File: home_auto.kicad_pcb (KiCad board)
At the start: 6 copper layers, 36.8 x 32.2 mm, 85 parts, among them J1 DF12NC_3.0_-60DS-0.5V_51_, J13 Conn_01x08_Pin, J2 DF12NC_3.0_-60DS-0.5V_51_, U1 RP115H331D, U3 RP115H181D, U4 LFMXO5-25

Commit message: relay unit
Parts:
- removed C13, C17, C18, C19, C20, C21, C22, C30, C31, C32, C33, C34, C35, C37, C38, C40, C41, C43, C45, C46, C47, C48, C49, C50, C52, C53, C55, C58, C59: 100n, Capacitor_SMD:C_0402_1005Metric
- removed C14, C24: 2.2u, Capacitor_SMD:C_0603_1608Metric
- removed C15, C28, C29, C36, C39, C51, C57, C60, C66: 10u, Capacitor_SMD:C_0603_1608Metric
- removed C16, C25, C26: 10u, Capacitor_SMD:C_0805_2012Metric
- removed C23, C27: 100n, Capacitor_SMD:C_0603_1608Metric
- removed C5: 0.1n, Capacitor_SMD:C_0603_1608Metric
- removed C6, C7: 22u, Capacitor_SMD:C_0805_2012Metric
- removed C8: 1u, Capacitor_SMD:C_0603_1608Metric
- removed C9: 3.3n, Capacitor_SMD:C_0603_1608Metric
- removed L1: SPM6530T-1R5M-HZ, SPM6530T-1R5M-HZ:SPM6530
- removed L10, L11, L2, L7, L9: MPZ1005S121CT000, Inductor_SMD:L_0402_1005Metric
- removed PS1: BD9D321EFJ-E2, BD9D321EFJ-E2:SOIC127P600X100-8N
- removed R184, R185: 1k, Resistor_SMD:R_0402_1005Metric
- removed R186, R187, R188, R189: 4.7k, Resistor_SMD:R_0402_1005Metric
- removed R190: 0R, Resistor_SMD:R_0603_1608Metric
- removed U3: RP115H181D, Package_TO_SOT_SMD:SOT-89-5
- removed U4: LFMXO5-25, Package_BGA:BGA-256_14.0x14.0mm_Layout16x16_P0.8mm_Ball0.45mm_Pad0.32mm_NSMD
- added D1: D_Zener_Dual_CommonCathode_AAK, Package_TO_SOT_SMD:SOT-23, B.Cu at (183.7, 75.1)
- added D10: D_Zener_Dual_CommonCathode_AAK, Package_TO_SOT_SMD:SOT-23, B.Cu at (163.8, 106.6)
- added D11: D_Zener_Dual_CommonCathode_AAK, Package_TO_SOT_SMD:SOT-23, B.Cu at (148.0, 106.6)
- added D12: D_Zener_Dual_CommonCathode_AAK, Package_TO_SOT_SMD:SOT-23, B.Cu at (195.5, 106.6)
- added D13: D_Zener_Dual_CommonCathode_AAK, Package_TO_SOT_SMD:SOT-23, B.Cu at (152.1, 75.0)
- added D14: D_Zener_Dual_CommonCathode_AAK, Package_TO_SOT_SMD:SOT-23, B.Cu at (136.2, 75.0)
- added D15: 5.0SMDJ6.0CAS, 5_0SMDJ6_0CAS:DIONM7959X262N, F.Cu at (73.1, 73.7)
- added D2: D_Zener_Dual_CommonCathode_AAK, Package_TO_SOT_SMD:SOT-23, B.Cu at (212.0, 75.1)
- added D3: D_Zener_Dual_CommonCathode_AAK, Package_TO_SOT_SMD:SOT-23, B.Cu at (167.9, 75.1)
- added D4: D_Zener_Dual_CommonCathode_AAK, Package_TO_SOT_SMD:SOT-23, B.Cu at (243.7, 75.2)
- added D5: D_Zener_Dual_CommonCathode_AAK, Package_TO_SOT_SMD:SOT-23, B.Cu at (227.9, 75.2)
- added D6: D_Zener_Dual_CommonCathode_AAK, Package_TO_SOT_SMD:SOT-23, B.Cu at (227.2, 106.6)
- added D7: D_Zener_Dual_CommonCathode_AAK, Package_TO_SOT_SMD:SOT-23, B.Cu at (243.0, 106.6)
- added D8: D_Zener_Dual_CommonCathode_AAK, Package_TO_SOT_SMD:SOT-23, B.Cu at (179.6, 106.6)
- added D9: D_Zener_Dual_CommonCathode_AAK, Package_TO_SOT_SMD:SOT-23, B.Cu at (211.3, 106.6)
- added J10: TC0203620000G, KiCad:TC0203620000G, F.Cu at (186.2, 46.5)
- added J11: TC0203620000G, KiCad:TC0203620000G, F.Cu at (214.5, 46.5)
- added J12: TC0203620000G, KiCad:TC0203620000G, F.Cu at (170.4, 46.4)
- added J14: TC0203620000G, KiCad:TC0203620000G, F.Cu at (230.3, 46.6)
- added J15: TC0203620000G, KiCad:TC0203620000G, F.Cu at (224.7, 135.3)
- added J16: TC0203620000G, KiCad:TC0203620000G, F.Cu at (240.5, 135.2)
- added J17: TC0203620000G, KiCad:TC0203620000G, F.Cu at (177.1, 135.2)
- added J18: TC0203620000G, KiCad:TC0203620000G, F.Cu at (208.9, 135.3)
- added J19: TC0203620000G, KiCad:TC0203620000G, F.Cu at (161.3, 135.3)
- added J20: TC0203620000G, KiCad:TC0203620000G, F.Cu at (145.5, 135.2)
- added J21: TC0203620000G, KiCad:TC0203620000G, F.Cu at (193.0, 135.2)
- added J22: TC0203620000G, KiCad:TC0203620000G, F.Cu at (154.5, 46.4)
- added J23: TC0203620000G, KiCad:TC0203620000G, F.Cu at (138.7, 46.4)
- added J24: Conn_01x02_Pin, Connector_PinHeader_1.27mm:PinHeader_1x02_P1.27mm_Vertical, F.Cu at (79.2, 66.2)
- added J25: Conn_01x04_Pin, Connector_PinHeader_1.27mm:PinHeader_1x04_P1.27mm_Vertical, F.Cu at (80.9, 56.6)
- added J26: Conn_01x02_Pin, Connector_PinHeader_1.27mm:PinHeader_1x02_P1.27mm_Vertical, F.Cu at (76.7, 56.6)
- added J27: TC0203620000G, KiCad:TC0203620000G, F.Cu at (60.6, 68.3)
- added J3: TC0203620000G, KiCad:TC0203620000G, F.Cu at (124.0, 61.3)
- added J4: Conn_02x10_Top_Bottom, Connector_PinHeader_2.54mm:PinHeader_2x10_P2.54mm_Vertical_SMD, F.Cu at (72.6, 107.7)
- added J5: Conn_02x10_Top_Bottom, Connector_PinHeader_2.54mm:PinHeader_2x10_P2.54mm_Vertical_SMD, F.Cu at (77.5, 90.2)
- added J6: TC0203620000G, KiCad:TC0203620000G, F.Cu at (256.7, 61.3)
- added J7: TC0203620000G, KiCad:TC0203620000G, F.Cu at (135.0, 117.5)
- added J8: TC0203620000G, KiCad:TC0203620000G, F.Cu at (256.2, 124.6)
- added J9: Conn_01x08_Pin, Connector_PinHeader_1.27mm:PinHeader_1x08_P1.27mm_Vertical, F.Cu at (233.5, 86.1)
- added K1: G5NB-1A4_DC5, G5NB-1A4_DC5:G5NB1A4DC5, F.Cu at (179.7, 72.5)
- added K10: G5NB-1A4_DC5, G5NB-1A4_DC5:G5NB1A4DC5, F.Cu at (231.8, 72.6)
- added K11: G5NB-1A4_DC5, G5NB-1A4_DC5:G5NB1A4DC5, F.Cu at (231.2, 109.2)
- added K12: G5NB-1A4_DC5, G5NB-1A4_DC5:G5NB1A4DC5, F.Cu at (223.3, 109.2)
- added K13: G5NB-1A4_DC5, G5NB-1A4_DC5:G5NB1A4DC5, F.Cu at (247.0, 109.2)
- added K14: G5NB-1A4_DC5, G5NB-1A4_DC5:G5NB1A4DC5, F.Cu at (239.1, 109.2)
- added K15: G5NB-1A4_DC5, G5NB-1A4_DC5:G5NB1A4DC5, F.Cu at (183.6, 109.2)
- added K16: G5NB-1A4_DC5, G5NB-1A4_DC5:G5NB1A4DC5, F.Cu at (175.7, 109.2)
- added K17: G5NB-1A4_DC5, G5NB-1A4_DC5:G5NB1A4DC5, F.Cu at (215.3, 109.2)
- added K18: G5NB-1A4_DC5, G5NB-1A4_DC5:G5NB1A4DC5, F.Cu at (207.4, 109.2)
- added K19: G5NB-1A4_DC5, G5NB-1A4_DC5:G5NB1A4DC5, F.Cu at (167.8, 109.2)
- added K2: G5NB-1A4_DC5, G5NB-1A4_DC5:G5NB1A4DC5, F.Cu at (187.6, 72.5)
- added K20: G5NB-1A4_DC5, G5NB-1A4_DC5:G5NB1A4DC5, F.Cu at (159.9, 109.2)
- added K21: G5NB-1A4_DC5, G5NB-1A4_DC5:G5NB1A4DC5, F.Cu at (152.0, 109.2)
- added K22: G5NB-1A4_DC5, G5NB-1A4_DC5:G5NB1A4DC5, F.Cu at (144.1, 109.2)
- added K23: G5NB-1A4_DC5, G5NB-1A4_DC5:G5NB1A4DC5, F.Cu at (199.5, 109.2)
- added K24: G5NB-1A4_DC5, G5NB-1A4_DC5:G5NB1A4DC5, F.Cu at (191.6, 109.2)
- added K25: G5NB-1A4_DC5, G5NB-1A4_DC5:G5NB1A4DC5, F.Cu at (148.1, 72.5)
- added K26: G5NB-1A4_DC5, G5NB-1A4_DC5:G5NB1A4DC5, F.Cu at (156.0, 72.5)
- added K27: G5NB-1A4_DC5, G5NB-1A4_DC5:G5NB1A4DC5, F.Cu at (132.2, 72.4)
- added K28: G5NB-1A4_DC5, G5NB-1A4_DC5:G5NB1A4DC5, F.Cu at (140.2, 72.4)
- added K3: G5NB-1A4_DC5, G5NB-1A4_DC5:G5NB1A4DC5, F.Cu at (208.0, 72.5)
- added K4: G5NB-1A4_DC5, G5NB-1A4_DC5:G5NB1A4DC5, F.Cu at (215.9, 72.5)
- added K5: G5NB-1A4_DC5, G5NB-1A4_DC5:G5NB1A4DC5, F.Cu at (163.9, 72.5)
- added K6: G5NB-1A4_DC5, G5NB-1A4_DC5:G5NB1A4DC5, F.Cu at (171.8, 72.5)
- added K7: G5NB-1A4_DC5, G5NB-1A4_DC5:G5NB1A4DC5, F.Cu at (239.7, 72.7)
- added K8: G5NB-1A4_DC5, G5NB-1A4_DC5:G5NB1A4DC5, F.Cu at (247.6, 72.7)
- added K9: G5NB-1A4_DC5, G5NB-1A4_DC5:G5NB1A4DC5, F.Cu at (223.9, 72.6)
- added Q1: BC849, Package_TO_SOT_SMD:SOT-23, B.Cu at (177.6, 75.1)
- added Q10: BC849, Package_TO_SOT_SMD:SOT-23, B.Cu at (233.9, 75.2)
- added Q11: BC849, Package_TO_SOT_SMD:SOT-23, B.Cu at (233.3, 106.6)
- added Q12: BC849, Package_TO_SOT_SMD:SOT-23, B.Cu at (221.1, 106.6)
- added Q13: BC849, Package_TO_SOT_SMD:SOT-23, B.Cu at (249.0, 106.6)
- added Q14: BC849, Package_TO_SOT_SMD:SOT-23, B.Cu at (236.9, 106.6)
- added Q15: BC849, Package_TO_SOT_SMD:SOT-23, B.Cu at (185.7, 106.6)
- added Q16: BC849, Package_TO_SOT_SMD:SOT-23, B.Cu at (173.5, 106.6)
- added Q17: BC849, Package_TO_SOT_SMD:SOT-23, B.Cu at (217.4, 106.6)
- added Q18: BC849, Package_TO_SOT_SMD:SOT-23, B.Cu at (205.3, 106.6)
- added Q19: BC849, Package_TO_SOT_SMD:SOT-23, B.Cu at (169.9, 106.6)
- added Q2: BC849, Package_TO_SOT_SMD:SOT-23, B.Cu at (189.8, 75.1)
- added Q20: BC849, Package_TO_SOT_SMD:SOT-23, B.Cu at (157.7, 106.6)
- added Q21: BC849, Package_TO_SOT_SMD:SOT-23, B.Cu at (154.1, 106.6)
- added Q22: BC849, Package_TO_SOT_SMD:SOT-23, B.Cu at (141.9, 106.6)
- added Q23: BC849, Package_TO_SOT_SMD:SOT-23, B.Cu at (201.5, 106.6)
- added Q24: BC849, Package_TO_SOT_SMD:SOT-23, B.Cu at (189.4, 106.6)
- added Q25: BC849, Package_TO_SOT_SMD:SOT-23, B.Cu at (146.0, 75.0)
- added Q26: BC849, Package_TO_SOT_SMD:SOT-23, B.Cu at (158.1, 75.0)
- added Q27: BC849, Package_TO_SOT_SMD:SOT-23, B.Cu at (130.2, 75.0)
- added Q28: BC849, Package_TO_SOT_SMD:SOT-23, B.Cu at (142.3, 75.0)
- added Q3: BC849, Package_TO_SOT_SMD:SOT-23, B.Cu at (205.9, 75.1)
- added Q4: BC849, Package_TO_SOT_SMD:SOT-23, B.Cu at (218.1, 75.1)
- added Q5: BC849, Package_TO_SOT_SMD:SOT-23, B.Cu at (161.8, 75.1)
- added Q6: BC849, Package_TO_SOT_SMD:SOT-23, B.Cu at (174.0, 75.1)
- added Q7: BC849, Package_TO_SOT_SMD:SOT-23, B.Cu at (237.6, 75.2)
- added Q8: BC849, Package_TO_SOT_SMD:SOT-23, B.Cu at (249.8, 75.2)
- added Q9: BC849, Package_TO_SOT_SMD:SOT-23, B.Cu at (221.8, 75.2)
- added R14: 4K7, Resistor_SMD:R_0603_1608Metric, F.Cu at (201.7, 86.1)
- added R15: 0R, Resistor_SMD:R_0805_2012Metric, F.Cu at (230.4, 84.3)
- added R16: 4K7, Resistor_SMD:R_0603_1608Metric, F.Cu at (207.9, 98.0)
- added R17: 4K7, Resistor_SMD:R_0603_1608Metric, F.Cu at (200.3, 86.1)
- added R18: 0R, Resistor_SMD:R_0603_1608Metric, F.Cu at (226.9, 85.1)
- added R19: 4K7, Resistor_SMD:R_0603_1608Metric, F.Cu at (209.4, 98.0)
- added R20: 4K7, Resistor_SMD:R_0603_1608Metric, F.Cu at (198.8, 86.1)
- added R21: 4K7, Resistor_SMD:R_0603_1608Metric, F.Cu at (210.9, 98.0)
- added R22: 4K7, Resistor_SMD:R_0603_1608Metric, F.Cu at (197.3, 86.1)
- added R23: 10k, Resistor_SMD:R_0603_1608Metric, B.Cu at (180.8, 75.5)
- added R24: 10k, Resistor_SMD:R_0603_1608Metric, B.Cu at (186.8, 75.5)
- added R25: 10k, Resistor_SMD:R_0603_1608Metric, B.Cu at (209.1, 75.5)
- added R26: 10k, Resistor_SMD:R_0603_1608Metric, B.Cu at (215.1, 75.5)
- added R27: 10k, Resistor_SMD:R_0603_1608Metric, B.Cu at (164.9, 75.5)
- added R28: 10k, Resistor_SMD:R_0603_1608Metric, B.Cu at (171.0, 75.5)
- added R29: 10k, Resistor_SMD:R_0603_1608Metric, B.Cu at (240.7, 75.7)
- added R30: 10k, Resistor_SMD:R_0603_1608Metric, B.Cu at (246.8, 75.7)
- added R31: 10k, Resistor_SMD:R_0603_1608Metric, B.Cu at (224.9, 75.6)
- added R32: 10k, Resistor_SMD:R_0603_1608Metric, B.Cu at (231.0, 75.6)
- added R33: 10k, Resistor_SMD:R_0603_1608Metric, B.Cu at (230.2, 106.2)
- added R34: 10k, Resistor_SMD:R_0603_1608Metric, B.Cu at (224.1, 106.2)
- added R35: 10k, Resistor_SMD:R_0603_1608Metric, B.Cu at (245.9, 106.2)
- added R36: 10k, Resistor_SMD:R_0603_1608Metric, B.Cu at (239.8, 106.2)
- added R37: 10k, Resistor_SMD:R_0603_1608Metric, B.Cu at (182.6, 106.2)
- added R38: 10k, Resistor_SMD:R_0603_1608Metric, B.Cu at (176.5, 106.2)
- added R39: 10k, Resistor_SMD:R_0603_1608Metric, B.Cu at (214.3, 106.2)
- added R40: 10k, Resistor_SMD:R_0603_1608Metric, B.Cu at (208.2, 106.2)
- added R41: 10k, Resistor_SMD:R_0603_1608Metric, B.Cu at (166.8, 106.2)
- added R42: 10k, Resistor_SMD:R_0603_1608Metric, B.Cu at (160.7, 106.2)
- added R43: 10k, Resistor_SMD:R_0603_1608Metric, B.Cu at (151.0, 106.2)
- added R44: 10k, Resistor_SMD:R_0603_1608Metric, B.Cu at (144.9, 106.2)
- added R45: 10k, Resistor_SMD:R_0603_1608Metric, B.Cu at (198.4, 106.2)
- added R46: 10k, Resistor_SMD:R_0603_1608Metric, B.Cu at (192.3, 106.2)
- added R47: 10k, Resistor_SMD:R_0603_1608Metric, B.Cu at (149.1, 75.5)
- added R48: 10k, Resistor_SMD:R_0603_1608Metric, B.Cu at (155.2, 75.5)
- added R49: 10k, Resistor_SMD:R_0603_1608Metric, B.Cu at (133.3, 75.4)
- added R50: 10k, Resistor_SMD:R_0603_1608Metric, B.Cu at (139.4, 75.4)
- added R51: 10k, Resistor_SMD:R_0603_1608Metric, F.Cu at (251.4, 103.6)
- added R52: 10k, Resistor_SMD:R_0603_1608Metric, F.Cu at (252.0, 78.5)
- added R53: 10k, Resistor_SMD:R_0603_1608Metric, F.Cu at (245.6, 98.6)
- added R54: 10k, Resistor_SMD:R_0603_1608Metric, F.Cu at (67.9, 63.6)
- added R55: 10k, Resistor_SMD:R_0603_1608Metric, F.Cu at (67.9, 66.1)
- added R8: 4K7, Resistor_SMD:R_0603_1608Metric, F.Cu at (206.1, 86.1)
- added R9: 4K7, Resistor_SMD:R_0603_1608Metric, F.Cu at (203.3, 98.0)
- added SW1: SW_Omron_B3FS, Button_Switch_SMD:SW_SPST_Omron_B3FS-105xP, F.Cu at (240.5, 85.3)
- added U2: ESP32-C3-WROOM-02, RF_Module:ESP32-C3-WROOM-02, F.Cu at (254.1, 90.6)
- C1: value 10u -> 100n; footprint Capacitor_SMD:C_0805_2012Metric -> Capacitor_SMD:C_0603_1608Metric; moved to F.Cu
- C2: value 10u -> 100n; footprint Capacitor_SMD:C_0805_2012Metric -> Capacitor_SMD:C_0603_1608Metric
- C3: value 1u -> 100n; footprint Capacitor_SMD:C_0402_1005Metric -> Capacitor_SMD:C_0603_1608Metric
- C4: value 100n -> 1u; footprint Capacitor_SMD:C_0402_1005Metric -> Capacitor_SMD:C_0603_1608Metric; moved to F.Cu
- J1, J2: value DF12NC_3.0_-60DS-0.5V_51_ -> TC0203620000G; footprint DF12NC_3.0_60DS-0.5V:HRS_DF12NC_3.0_-60DS-0.5V_51_ -> KiCad:TC0203620000G; moved to F.Cu
- J13: value Conn_01x08_Pin -> TC0203620000G; footprint Connector_PinHeader_1.27mm:PinHeader_1x08_P1.27mm_Vertical -> KiCad:TC0203620000G; moved to F.Cu
- R1: value 4.7k -> 4K7; moved to F.Cu
- R10, R4: value 4.7k -> 4K7
- R11, R13, R5, R7: value 0R -> 4K7
- R12, R6: value 29.7k -> 4K7
- R2: value 7.5k -> 4K7
- R3: value 22k -> 4K7
- U1: value RP115H331D -> MACHox5_board; footprint Package_TO_SOT_SMD:SOT-89-5 -> machox5_board:machox5_board
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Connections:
- C1 pad 1: +5V -> /ESP32/EN
- C2 pad 1: +5V -> +3V3_ESP
- C3 pad 1: +5V -> +3V3_ESP
- C4 pad 1: Net-(PS1-BOOT) -> /ESP32/EN
- C4 pad 2: Net-(PS1-SW) -> GND
- J1 pad 1: +1V8 -> 230VAC
- J1 pad 2: +3V3 -> 230VAC
- J13 pad 1: +3V3_BANK -> /led_cluster/led_cur_lim3/UP_OUT
- J13 pad 2: /FPGA_machX05/FTDI/NX_TDO -> /led_cluster/led_cur_lim3/DOWN_OUT
- J2 pad 1: GND -> 230VAC
- J2 pad 2: GND -> 230VAC
- R1 pad 1: +5V -> /sw_10
- R1 pad 2: Net-(PS1-EN) -> +UP
- R10 pad 1: +5V -> /sw_4
- R10 pad 2: Net-(U3-CE) -> +UP
- R11 pad 1: Net-(U3-VFB) -> /sw_15
- R11 pad 2: +1V8 -> +UP
- R12 pad 1: GND -> /sw_5
- R12 pad 2: Net-(U3-VFB) -> +UP
- R13 pad 1: Net-(U4N-VCCADC18) -> /sw_16
- R13 pad 2: GND -> +UP
- R2 pad 1: Net-(PS1-FB) -> /sw_0
- R2 pad 2: +1V0 -> +UP
- R3 pad 1: GND_DCDC -> /sw_11
- R3 pad 2: Net-(PS1-FB) -> +UP
- R4 pad 1: +5V -> /sw_1
- R4 pad 2: Net-(U1-CE) -> +UP
- R5 pad 1: Net-(U1-VFB) -> /sw_12
- R5 pad 2: +3V3 -> +UP
- R6 pad 1: GND -> /sw_2
- R6 pad 2: Net-(U1-VFB) -> +UP
- R7 pad 1: GND -> /sw_13
- R7 pad 2: GND_DCDC -> +UP
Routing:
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- added copper zone on F.Cu, net +UP
- added copper zone on B.Cu, net /led_cluster/led_cur_lim/DOWN_OUT
- added copper zone on F.Cu, net /led_cluster/led_cur_lim/DOWN_OUT
- added copper zone on B.Cu, net /led_cluster/led_cur_lim/UP_OUT
- added copper zone on F.Cu, net /led_cluster/led_cur_lim/UP_OUT
- added copper zone on B.Cu, net /led_cluster/led_cur_lim1/DOWN_OUT
- added copper zone on F.Cu, net /led_cluster/led_cur_lim1/DOWN_OUT
- added copper zone on B.Cu, net /led_cluster/led_cur_lim1/UP_OUT
- added copper zone on F.Cu, net /led_cluster/led_cur_lim1/UP_OUT
- added copper zone on B.Cu, net /led_cluster/led_cur_lim2/DOWN_OUT
- added copper zone on F.Cu, net /led_cluster/led_cur_lim2/DOWN_OUT
- added copper zone on B.Cu, net /led_cluster/led_cur_lim2/UP_OUT
- added copper zone on F.Cu, net /led_cluster/led_cur_lim2/UP_OUT
- added copper zone on B.Cu, net /led_cluster/led_cur_lim3/DOWN_OUT
- added copper zone on F.Cu, net /led_cluster/led_cur_lim3/DOWN_OUT
- added copper zone on B.Cu, net /led_cluster/led_cur_lim3/UP_OUT
- added copper zone on F.Cu, net /led_cluster/led_cur_lim3/UP_OUT
- added copper zone on B.Cu, net /led_cluster/led_cur_lim4/DOWN_OUT
- added copper zone on F.Cu, net /led_cluster/led_cur_lim4/DOWN_OUT
- added copper zone on B.Cu, net /led_cluster/led_cur_lim4/UP_OUT
- added copper zone on F.Cu, net /led_cluster/led_cur_lim4/UP_OUT
- added copper zone on B.Cu, net /led_cluster1/led_cur_lim/DOWN_OUT
- added copper zone on F.Cu, net /led_cluster1/led_cur_lim/DOWN_OUT
- added copper zone on B.Cu, net /led_cluster1/led_cur_lim/UP_OUT
- added copper zone on F.Cu, net /led_cluster1/led_cur_lim/UP_OUT
- added copper zone on B.Cu, net /led_cluster1/led_cur_lim1/DOWN_OUT
- added copper zone on F.Cu, net /led_cluster1/led_cur_lim1/DOWN_OUT
- added copper zone on B.Cu, net /led_cluster1/led_cur_lim1/UP_OUT
- added copper zone on F.Cu, net /led_cluster1/led_cur_lim1/UP_OUT
- added copper zone on B.Cu, net /led_cluster1/led_cur_lim2/DOWN_OUT
- added copper zone on F.Cu, net /led_cluster1/led_cur_lim2/DOWN_OUT
- added copper zone on B.Cu, net /led_cluster1/led_cur_lim2/UP_OUT
- added copper zone on F.Cu, net /led_cluster1/led_cur_lim2/UP_OUT
- added copper zone on B.Cu, net /led_cluster1/led_cur_lim3/DOWN_OUT
- added copper zone on F.Cu, net /led_cluster1/led_cur_lim3/DOWN_OUT
- added copper zone on B.Cu, net /led_cluster1/led_cur_lim3/UP_OUT
- added copper zone on F.Cu, net /led_cluster1/led_cur_lim3/UP_OUT
- added copper zone on B.Cu, net /led_cluster1/led_cur_lim4/DOWN_OUT
- added copper zone on F.Cu, net /led_cluster1/led_cur_lim4/DOWN_OUT
- added copper zone on B.Cu, net /led_cluster1/led_cur_lim4/UP_OUT
- added copper zone on F.Cu, net /led_cluster1/led_cur_lim4/UP_OUT
- added copper zone on B.Cu, net /led_cur_lim5/DOWN_OUT
- added copper zone on F.Cu, net /led_cur_lim5/DOWN_OUT
- added copper zone on B.Cu, net /led_cur_lim5/UP_OUT
- added copper zone on F.Cu, net /led_cur_lim5/UP_OUT
- added copper zone on B.Cu, net /led_cur_lim7/DOWN_OUT
- added copper zone on F.Cu, net /led_cur_lim7/DOWN_OUT
- added copper zone on B.Cu, net /led_cur_lim7/UP_OUT
- added copper zone on F.Cu, net /led_cur_lim7/UP_OUT
- added copper zone on B.Cu, net /led_cur_lim8/DOWN_OUT
- added copper zone on F.Cu, net /led_cur_lim8/DOWN_OUT
- added copper zone on B.Cu, net /led_cur_lim8/UP_OUT
- added copper zone on F.Cu, net /led_cur_lim8/UP_OUT
- added copper zone on F.Cu, net 230VAC
- removed copper zone on B.Cu, net +1V0
- removed copper zone on F.Cu, net +1V0
- removed copper zone on In2.Cu, net +1V0
- removed copper zone on B.Cu, net +1V8
- removed copper zone on F.Cu, net +1V8
- removed copper zone on In3.Cu, net +1V8
- removed copper zone on F.Cu, net +1V8_BANK
- removed copper zone on In2.Cu, net +1V8_BANK
- removed copper zone on In3.Cu, net +1V8_BANK
- removed copper zone on B.Cu, net +3V3
- removed copper zone on F.Cu, net +3V3
- removed copper zone on In2.Cu, net +3V3
- removed copper zone on F.Cu, net +3V3_BANK
- removed copper zone on In2.Cu, net +3V3_BANK
- removed copper zone on In3.Cu, net +3V3_BANK
- removed copper zone on B.Cu, net +5V
- removed copper zone on F.Cu, net +5V
- removed copper zone on In2.Cu, net +5V
- removed copper zone on In3.Cu, net +5V
- removed copper zone on B.Cu, net GND
- removed copper zone on F.Cu, net GND
- removed copper zone on In1.Cu, net GND
- removed copper zone on In2.Cu, net GND
- removed copper zone on In3.Cu, net GND
- removed copper zone on In4.Cu, net GND
- removed copper zone on F.Cu, net GND_DCDC
- removed copper zone on F.Cu, net Net-(PS1-SW)
- removed copper zone on F.Cu, net VCC_AUX
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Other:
- board size 36.8 x 32.2 mm -> 142.4 x 97.4 mm
- copper layers 6 -> 2

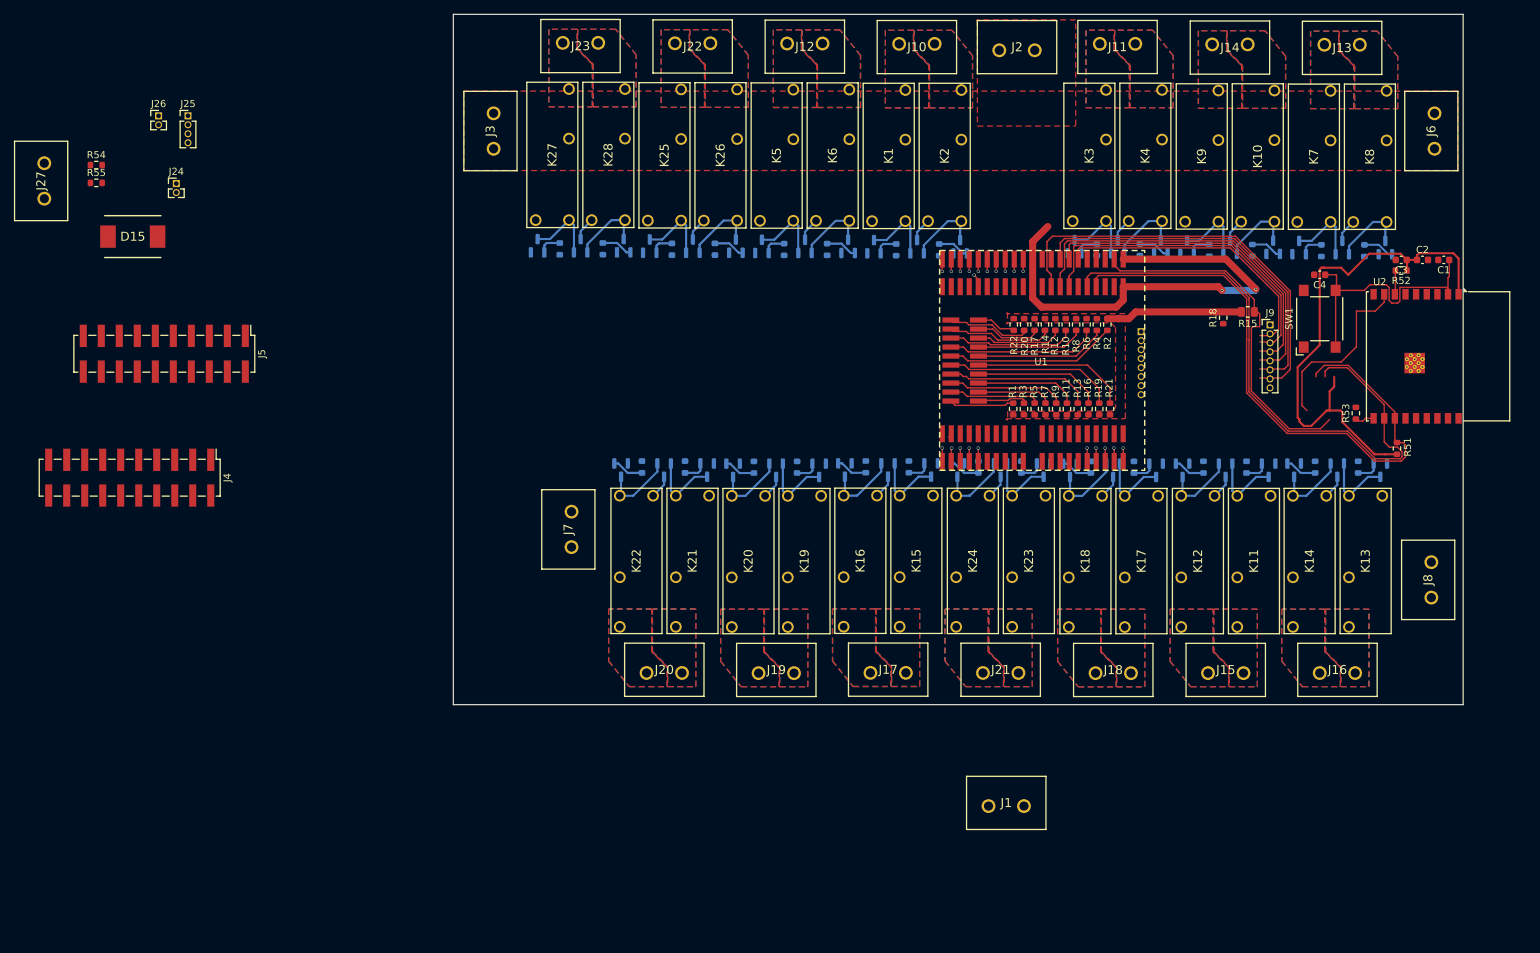
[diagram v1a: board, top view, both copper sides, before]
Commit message: relay placment
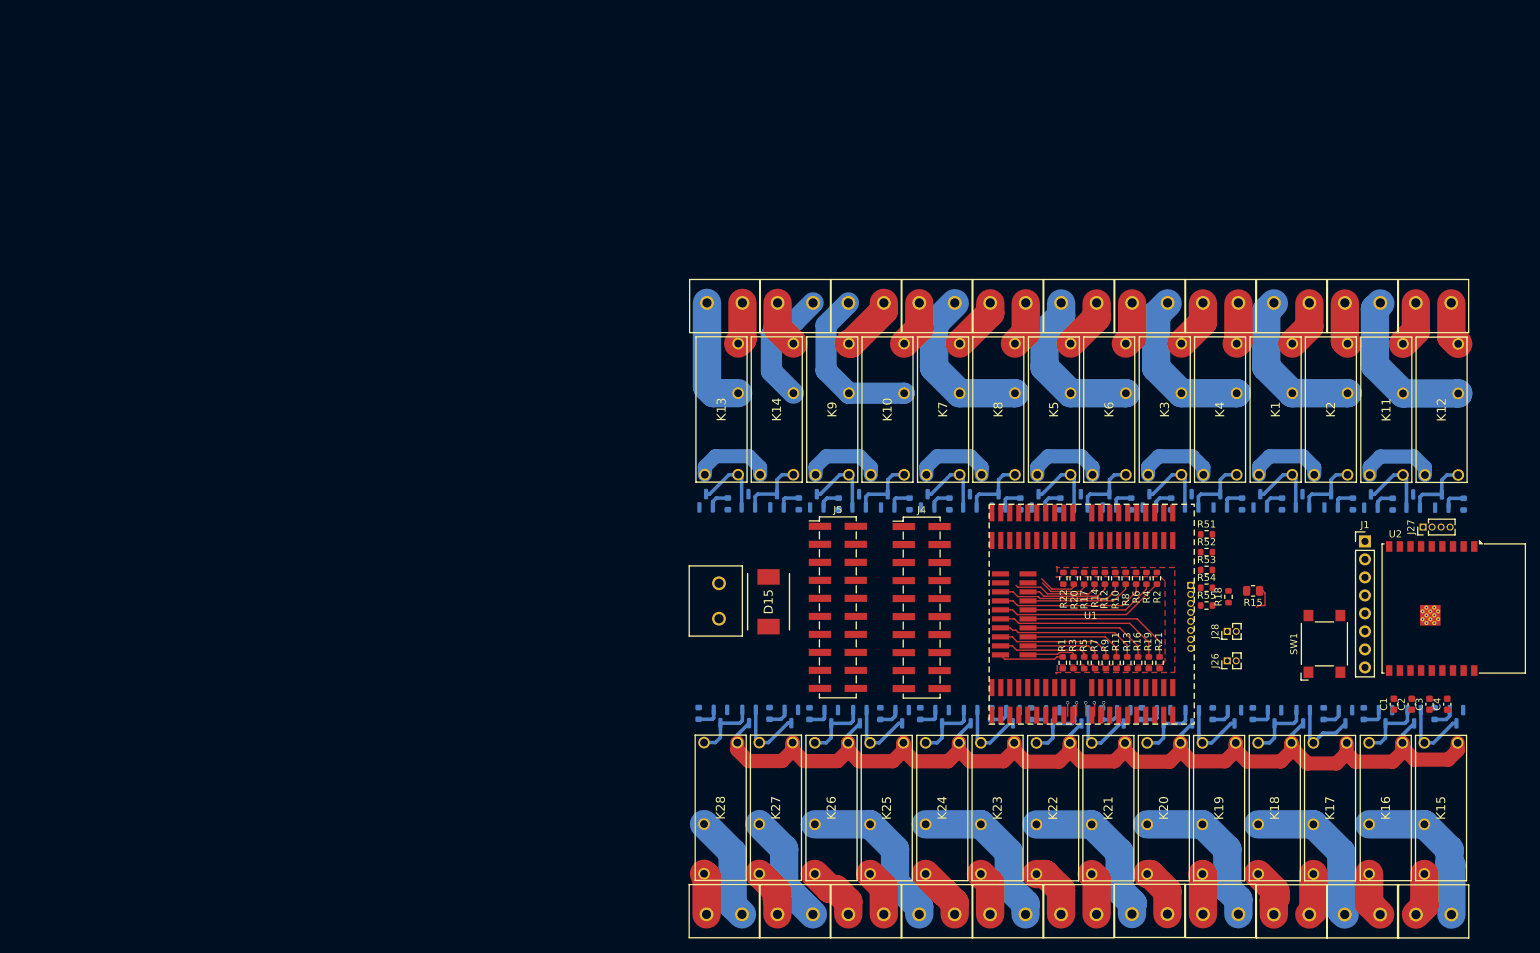
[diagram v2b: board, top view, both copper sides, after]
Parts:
- added J28: Conn_01x02_Pin, Connector_PinHeader_1.27mm:PinHeader_1x02_P1.27mm_Vertical, F.Cu at (227.4, 129.4)
- added J29: TC0203620000G, KiCad:TC0203620000G, F.Cu at (155.8, 127.6)
- J1: value TC0203620000G -> Conn_01x08_Pin; footprint KiCad:TC0203620000G -> Connector_PinHeader_2.54mm:PinHeader_1x08_P2.54mm_Vertical
- J10, J11, J12, J13, J14, J15, J16, J17, J18, J19, J2, J20, J21, J22, J23, J3, J6, J7, J8: value TC0203620000G -> Screw_Terminal_01x02
- J24: value Conn_01x02_Pin -> Screw_Terminal_01x02; footprint Connector_PinHeader_1.27mm:PinHeader_1x02_P1.27mm_Vertical -> KiCad:TC0203620000G
- J25: value Conn_01x04_Pin -> Screw_Terminal_01x02; footprint Connector_PinHeader_1.27mm:PinHeader_1x04_P1.27mm_Vertical -> KiCad:TC0203620000G
- J27: value TC0203620000G -> Conn_01x04_Pin; footprint KiCad:TC0203620000G -> Connector_PinHeader_1.27mm:PinHeader_1x04_P1.27mm_Vertical
- J9: value Conn_01x08_Pin -> Screw_Terminal_01x02; footprint Connector_PinHeader_1.27mm:PinHeader_1x08_P1.27mm_Vertical -> KiCad:TC0203620000G
- moved J27 199.9 mm to (255.1, 114.7)
- moved J26 169.2 mm to (227.4, 133.5), turned to 90 degrees
- moved R54 167.6 mm to (224.5, 123.2)
- moved R55 167.6 mm to (224.5, 125.7)
- moved J25 134.3 mm to (154.0, 169.3)
- moved J24 133.5 mm to (164.0, 169.3)
- moved J23 127.9 mm to (174.0, 169.3), turned to 0 degrees
- moved J3 127.0 mm to (249.0, 83.0), turned to 180 degrees
- moved J22 126.4 mm to (184.0, 169.3), turned to 0 degrees
- moved J4 113.2 mm to (184.3, 126.0), turned to 0 degrees
- moved D15 103.4 mm to (162.8, 125.2), turned to -90 degrees
- moved J5 101.5 mm to (172.5, 126.0), turned to 0 degrees
- moved J7 100.2 mm to (229.0, 83.0), turned to 180 degrees
- moved Q13 95.2 mm to (153.9, 110.9), turned to 90 degrees
- moved K13 90.9 mm to (156.1, 108.3), turned to 90 degrees
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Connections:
- net /led_cluster/led_cur_lim/DOWN_R renamed /led_cur_lim2/DOWN_R
- net /led_cluster/led_cur_lim/UP_R renamed /led_cur_lim2/UP_R
- net /led_cluster/led_cur_lim1/DOWN_R renamed /led_cur_lim3/DOWN_R
- net /led_cluster/led_cur_lim1/UP_R renamed /led_cur_lim3/UP_R
- net /led_cluster/led_cur_lim2/DOWN_R renamed /led_cur_lim4/DOWN_R
- net /led_cluster/led_cur_lim2/UP_R renamed /led_cur_lim4/UP_R
- net /led_cluster1/led_cur_lim1/DOWN_R renamed /led_cur_lim1/DOWN_R
- net /led_cluster1/led_cur_lim1/UP_R renamed /led_cur_lim1/UP_R
- net /led_cluster1/led_cur_lim2/DOWN_R renamed /led_cur_lim9/DOWN_R
- net /led_cluster1/led_cur_lim2/UP_R renamed /led_cur_lim9/UP_R
- net /led_cluster1/led_cur_lim4/DOWN_R renamed /led_cur_lim10/DOWN_R
- net /led_cluster1/led_cur_lim4/UP_R renamed /led_cur_lim10/UP_R
- net /led_cur_lim5/DOWN_OUT renamed /out_B0
- net /led_cur_lim5/UP_OUT renamed /out_B1
- D11 pad 1: /led_cur_lim5/UP_R -> /led_cur_lim11/UP_R
- D11 pad 2: /led_cur_lim5/DOWN_R -> /led_cur_lim11/DOWN_R
- D12 pad 1: /led_cur_lim6/UP_R -> /led_cur_lim12/UP_R
- D12 pad 2: /led_cur_lim6/DOWN_R -> /led_cur_lim12/DOWN_R
- D13 pad 1: /led_cur_lim7/UP_R -> /led_cur_lim13/UP_R
- D13 pad 2: /led_cur_lim7/DOWN_R -> /led_cur_lim13/DOWN_R
- D14 pad 1: /led_cur_lim8/UP_R -> /led_cur_lim14/UP_R
- D14 pad 2: /led_cur_lim8/DOWN_R -> /led_cur_lim14/DOWN_R
- D4 pad 1: /led_cluster/led_cur_lim3/UP_R -> /led_cur_lim5/UP_R
- D4 pad 2: /led_cluster/led_cur_lim3/DOWN_R -> /led_cur_lim5/DOWN_R
- D5 pad 1: /led_cluster/led_cur_lim4/UP_R -> /led_cur_lim6/UP_R
- D5 pad 2: /led_cluster/led_cur_lim4/DOWN_R -> /led_cur_lim6/DOWN_R
- D7 pad 1: /led_cluster1/led_cur_lim/UP_R -> /led_cur_lim7/UP_R
- D7 pad 2: /led_cluster1/led_cur_lim/DOWN_R -> /led_cur_lim7/DOWN_R
- D8 pad 1: /led_cluster1/led_cur_lim3/UP_R -> /led_cur_lim8/UP_R
- D8 pad 2: /led_cluster1/led_cur_lim3/DOWN_R -> /led_cur_lim8/DOWN_R
- J1 pad 1: 230VAC -> +3V3
- J1 pad 2: 230VAC -> /mux_3
- J10 pad 1: /led_cluster/led_cur_lim/UP_OUT -> /out_51
- J10 pad 2: /led_cluster/led_cur_lim/DOWN_OUT -> /out_50
- J11 pad 1: /led_cluster/led_cur_lim1/UP_OUT -> /pwd_5
- J11 pad 2: /led_cluster/led_cur_lim1/DOWN_OUT -> /out_61
- J12 pad 1: /led_cluster/led_cur_lim2/UP_OUT -> /out_60
- J12 pad 2: /led_cluster/led_cur_lim2/DOWN_OUT -> /pwd_6
- J13 pad 1: /led_cluster/led_cur_lim3/UP_OUT -> /pwd_72
- J13 pad 2: /led_cluster/led_cur_lim3/DOWN_OUT -> /out_71
- J14 pad 1: /led_cluster/led_cur_lim4/UP_OUT -> /out_70
- J14 pad 2: /led_cluster/led_cur_lim4/DOWN_OUT -> /pwd_71
- J15 pad 1: /led_cluster1/led_cur_lim1/UP_OUT -> /out_80
- J15 pad 2: /led_cluster1/led_cur_lim1/DOWN_OUT -> /pwd_80
- J16 pad 1: /led_cluster1/led_cur_lim/UP_OUT -> /pwd_90
- J16 pad 2: /led_cluster1/led_cur_lim/DOWN_OUT -> /out_81
- J17 pad 1: /led_cluster1/led_cur_lim3/UP_OUT -> /out_91
- J17 pad 2: /led_cluster1/led_cur_lim3/DOWN_OUT -> /out_90
- J18 pad 1: /led_cluster1/led_cur_lim2/UP_OUT -> /out_A0
- J18 pad 2: /led_cluster1/led_cur_lim2/DOWN_OUT -> /pwd_A0
- J19 pad 1: /led_cluster1/led_cur_lim4/UP_OUT -> /pwd_B0
- J19 pad 2: /led_cluster1/led_cur_lim4/DOWN_OUT -> /out_A1
- J2 pad 1: 230VAC -> /out_11
- J2 pad 2: 230VAC -> /out_10
- J21 pad 1: /led_cur_lim6/UP_OUT -> /out_C0
- J21 pad 2: /led_cur_lim6/DOWN_OUT -> /pwd_C0
- J22 pad 1: /led_cur_lim7/UP_OUT -> /pwd_D0
- J22 pad 2: /led_cur_lim7/DOWN_OUT -> /out_C1
- J23 pad 1: /led_cur_lim8/UP_OUT -> /out_D1
- J23 pad 2: /led_cur_lim8/DOWN_OUT -> /out_D0
- J24 pad 1: +3V3_ESP -> /out_E0
- J24 pad 2: +3V3 -> /pwd_E0
- J25 pad 1: GND -> /out_E1
- J25 pad 2: /TX -> /pwd_E1
- J26 pad 1: Net-(J26-Pin_1) -> +3V3_ESP
- J26 pad 2: GND -> +3V3
- J27 pad 1: +5V -> GND
- J27 pad 2: GND -> /TX
- J3 pad 1: 230VAC -> /pwd_1
- J3 pad 2: 230VAC -> /out_21
- J6 pad 1: 230VAC -> /out_20
- J6 pad 2: 230VAC -> /pwd_2
- J7 pad 1: 230VAC -> /out_31
- J7 pad 2: 230VAC -> /out_30
- J8 pad 1: 230VAC -> /pwd_3
- J8 pad 2: 230VAC -> /out_41
- J9 pad 1: +3V3 -> /out_40
- J9 pad 2: /mux_3 -> /pwd_4
- K1 pad 2: 230VAC -> /pwd_2
- K1 pad 3: /led_cluster/led_cur_lim/DOWN_OUT -> /out_20
- K10 pad 1: /led_cluster/led_cur_lim4/UP_R -> /led_cur_lim6/UP_R
- K10 pad 2: 230VAC -> /pwd_6
- K10 pad 3: /led_cluster/led_cur_lim4/UP_OUT -> /out_61
- K11 pad 2: 230VAC -> /pwd_1
- K11 pad 3: /led_cluster1/led_cur_lim1/DOWN_OUT -> /out_10
- K12 pad 2: 230VAC -> /pwd_1
- K12 pad 3: /led_cluster1/led_cur_lim1/UP_OUT -> /out_11
- K13 pad 1: /led_cluster1/led_cur_lim/DOWN_R -> /led_cur_lim7/DOWN_R
- K13 pad 2: 230VAC -> /pwd_71
- K13 pad 3: /led_cluster1/led_cur_lim/DOWN_OUT -> /out_70
- K14 pad 1: /led_cluster1/led_cur_lim/UP_R -> /led_cur_lim7/UP_R
- K14 pad 2: 230VAC -> /pwd_72
- K14 pad 3: /led_cluster1/led_cur_lim/UP_OUT -> /out_71
- K15 pad 1: /led_cluster1/led_cur_lim3/DOWN_R -> /led_cur_lim8/DOWN_R
- K15 pad 2: 230VAC -> /pwd_80
- K15 pad 3: /led_cluster1/led_cur_lim3/DOWN_OUT -> /out_80
- K16 pad 1: /led_cluster1/led_cur_lim3/UP_R -> /led_cur_lim8/UP_R
- K16 pad 2: 230VAC -> /pwd_80
- K16 pad 3: /led_cluster1/led_cur_lim3/UP_OUT -> /out_81
- K17 pad 2: 230VAC -> /pwd_90
- K17 pad 3: /led_cluster1/led_cur_lim2/DOWN_OUT -> /out_90
- K18 pad 2: 230VAC -> /pwd_90
- K18 pad 3: /led_cluster1/led_cur_lim2/UP_OUT -> /out_91
- K19 pad 2: 230VAC -> /pwd_A0
- K19 pad 3: /led_cluster1/led_cur_lim4/DOWN_OUT -> /out_A0
- K2 pad 2: 230VAC -> /pwd_2
- K2 pad 3: /led_cluster/led_cur_lim/UP_OUT -> /out_21
- K20 pad 2: 230VAC -> /pwd_A0
- K20 pad 3: /led_cluster1/led_cur_lim4/UP_OUT -> /out_A1
- K21 pad 1: /led_cur_lim5/DOWN_R -> /led_cur_lim11/DOWN_R
- K21 pad 2: 230VAC -> /pwd_B0
- K22 pad 1: /led_cur_lim5/UP_R -> /led_cur_lim11/UP_R
- K22 pad 2: 230VAC -> /pwd_B0
- K23 pad 1: /led_cur_lim6/DOWN_R -> /led_cur_lim12/DOWN_R
- K23 pad 2: 230VAC -> /pwd_C0
- K23 pad 3: /led_cur_lim6/DOWN_OUT -> /out_C0
- K24 pad 1: /led_cur_lim6/UP_R -> /led_cur_lim12/UP_R
- K24 pad 2: 230VAC -> /pwd_C0
- K24 pad 3: /led_cur_lim6/UP_OUT -> /out_C1
- K25 pad 1: /led_cur_lim7/DOWN_R -> /led_cur_lim13/DOWN_R
- K25 pad 2: 230VAC -> /pwd_D0
- K25 pad 3: /led_cur_lim7/DOWN_OUT -> /out_D0
- K26 pad 1: /led_cur_lim7/UP_R -> /led_cur_lim13/UP_R
- K26 pad 2: 230VAC -> /pwd_D0
- K26 pad 3: /led_cur_lim7/UP_OUT -> /out_D1
- K27 pad 1: /led_cur_lim8/DOWN_R -> /led_cur_lim14/DOWN_R
- K27 pad 2: 230VAC -> /pwd_E0
- K27 pad 3: /led_cur_lim8/DOWN_OUT -> /out_E0
- K28 pad 1: /led_cur_lim8/UP_R -> /led_cur_lim14/UP_R
- K28 pad 2: 230VAC -> /pwd_E1
- K28 pad 3: /led_cur_lim8/UP_OUT -> /out_E1
- K3 pad 2: 230VAC -> /pwd_3
- K3 pad 3: /led_cluster/led_cur_lim1/DOWN_OUT -> /out_30
- K4 pad 2: 230VAC -> /pwd_3
- K4 pad 3: /led_cluster/led_cur_lim1/UP_OUT -> /out_31
- K5 pad 2: 230VAC -> /pwd_4
- K5 pad 3: /led_cluster/led_cur_lim2/DOWN_OUT -> /out_40
- K6 pad 2: 230VAC -> /pwd_4
- K6 pad 3: /led_cluster/led_cur_lim2/UP_OUT -> /out_41
- K7 pad 1: /led_cluster/led_cur_lim3/DOWN_R -> /led_cur_lim5/DOWN_R
- K7 pad 2: 230VAC -> /pwd_5
- K7 pad 3: /led_cluster/led_cur_lim3/DOWN_OUT -> /out_50
- K8 pad 1: /led_cluster/led_cur_lim3/UP_R -> /led_cur_lim5/UP_R
- K8 pad 2: 230VAC -> /pwd_5
- K8 pad 3: /led_cluster/led_cur_lim3/UP_OUT -> /out_51
- K9 pad 1: /led_cluster/led_cur_lim4/DOWN_R -> /led_cur_lim6/DOWN_R
- K9 pad 2: 230VAC -> /pwd_6
- K9 pad 3: /led_cluster/led_cur_lim4/DOWN_OUT -> /out_60
- Q10 pad 3: /led_cluster/led_cur_lim4/UP_R -> /led_cur_lim6/UP_R
- Q13 pad 3: /led_cluster1/led_cur_lim/DOWN_R -> /led_cur_lim7/DOWN_R
- Q14 pad 3: /led_cluster1/led_cur_lim/UP_R -> /led_cur_lim7/UP_R
- Q15 pad 3: /led_cluster1/led_cur_lim3/DOWN_R -> /led_cur_lim8/DOWN_R
- Q16 pad 3: /led_cluster1/led_cur_lim3/UP_R -> /led_cur_lim8/UP_R
- Q21 pad 3: /led_cur_lim5/DOWN_R -> /led_cur_lim11/DOWN_R
- Q22 pad 3: /led_cur_lim5/UP_R -> /led_cur_lim11/UP_R
- Q23 pad 3: /led_cur_lim6/DOWN_R -> /led_cur_lim12/DOWN_R
- Q24 pad 3: /led_cur_lim6/UP_R -> /led_cur_lim12/UP_R
- Q25 pad 3: /led_cur_lim7/DOWN_R -> /led_cur_lim13/DOWN_R
- Q26 pad 3: /led_cur_lim7/UP_R -> /led_cur_lim13/UP_R
- Q27 pad 3: /led_cur_lim8/DOWN_R -> /led_cur_lim14/DOWN_R
- Q28 pad 3: /led_cur_lim8/UP_R -> /led_cur_lim14/UP_R
- Q7 pad 3: /led_cluster/led_cur_lim3/DOWN_R -> /led_cur_lim5/DOWN_R
- Q8 pad 3: /led_cluster/led_cur_lim3/UP_R -> /led_cur_lim5/UP_R
- Q9 pad 3: /led_cluster/led_cur_lim4/DOWN_R -> /led_cur_lim6/DOWN_R
- R23 pad 2: /UP_10 -> /led_cur_lim2/UP
- R24 pad 2: /DOWN_10 -> /led_cur_lim2/DOWN
- R25 pad 2: /UP_11 -> /led_cur_lim3/UP
- R26 pad 2: /DOWN_11 -> /led_cur_lim3/DOWN
- R27 pad 2: /UP_12 -> /led_cur_lim4/UP
- R28 pad 2: /DOWN_12 -> /led_cur_lim4/DOWN
- R29 pad 2: /UP_13 -> /led_cur_lim5/UP
- R30 pad 2: /DOWN_13 -> /led_cur_lim5/DOWN
- R31 pad 2: /UP_14 -> /led_cur_lim6/UP
- R32 pad 2: /DOWN_14 -> /led_cur_lim6/DOWN
- R33 pad 2: /led_cluster1/UP1 -> /led_cur_lim1/UP
- R34 pad 2: /led_cluster1/DOWN1 -> /led_cur_lim1/DOWN
- R35 pad 2: /led_cluster1/UP0 -> /led_cur_lim7/UP
- R36 pad 2: /led_cluster1/DOWN0 -> /led_cur_lim7/DOWN
- R37 pad 2: /led_cluster1/UP3 -> /led_cur_lim8/UP
- R38 pad 2: /led_cluster1/DOWN3 -> /led_cur_lim8/DOWN
- R39 pad 2: /led_cluster1/UP2 -> /led_cur_lim9/UP
- R40 pad 2: /led_cluster1/DOWN2 -> /led_cur_lim9/DOWN
- R41 pad 2: /led_cluster1/UP4 -> /led_cur_lim10/UP
- R42 pad 2: /led_cluster1/DOWN4 -> /led_cur_lim10/DOWN
- R43 pad 2: /led_cur_lim5/UP -> /led_cur_lim11/UP
- R44 pad 2: /led_cur_lim5/DOWN -> /led_cur_lim11/DOWN
- R45 pad 2: /led_cur_lim6/UP -> /led_cur_lim12/UP
- R46 pad 2: /led_cur_lim6/DOWN -> /led_cur_lim12/DOWN
- R47 pad 2: /led_cur_lim7/UP -> /led_cur_lim13/UP
- R48 pad 2: /led_cur_lim7/DOWN -> /led_cur_lim13/DOWN
- R49 pad 2: /led_cur_lim8/UP -> /led_cur_lim14/UP
- R50 pad 2: /led_cur_lim8/DOWN -> /led_cur_lim14/DOWN
- U1 pad C17: /led_cur_lim8/UP -> unconnected-(U1B-GPIO31-PadC17)
- U1 pad C19: /led_cur_lim8/DOWN -> unconnected-(U1B-GPIO33-PadC19)
- U1 pad C7: /led_cur_lim6/UP -> unconnected-(U1B-GPIO21-PadC7)
- U1 pad C9: /led_cur_lim6/DOWN -> unconnected-(U1B-GPIO23-PadC9)
- U1 pad E0: /led_cur_lim5/DOWN -> unconnected-(U1D-GPIO54-PadE0)
- U1 pad E1: /led_cluster1/UP4 -> unconnected-(U1D-GPIO55-PadE1)
- U1 pad E2: /led_cur_lim5/UP -> unconnected-(U1D-GPIO56-PadE2)
- U1 pad E3: /led_cluster1/DOWN4 -> unconnected-(U1D-GPIO57-PadE3)
- U1 pad E5: /led_cluster1/UP3 -> unconnected-(U1D-GPIO59-PadE5)
- U1 pad E6: /led_cur_lim7/DOWN -> unconnected-(U1D-GPIO60-PadE6)
- U1 pad E7: /led_cluster1/DOWN3 -> unconnected-(U1D-GPIO61-PadE7)
- U1 pad E8: /led_cur_lim7/UP -> unconnected-(U1D-GPIO62-PadE8)
- U1 pad E9: /led_cluster1/UP2 -> unconnected-(U1D-GPIO63-PadE9)
- U1 pad F11: /led_cluster1/DOWN2 -> unconnected-(U1E-GPIO65-PadF11)
- U1 pad F13: /led_cluster1/UP1 -> unconnected-(U1E-GPIO67-PadF13)
- U1 pad F15: /led_cluster1/DOWN1 -> unconnected-(U1E-GPIO69-PadF15)
- U1 pad F17: /led_cluster1/UP0 -> unconnected-(U1E-GPIO71-PadF17)
- U1 pad F19: /led_cluster1/DOWN0 -> unconnected-(U1E-GPIO73-PadF19)
- U2 pad 8: Net-(J26-Pin_1) -> Net-(J28-Pin_1)
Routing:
- net +5V: track 112.4 -> 247.3 mm, vias 2 -> 0
- net /TX: track 86.1 -> 0.00 mm
- net /RX: track 85.4 -> 0.00 mm
- net +3V3_ESP: track 75.5 -> 0.00 mm
- net /mux_4: track 60.3 -> 0.00 mm
- net /mux_0: track 53.3 -> 0.00 mm
- net /mux_5: track 52.0 -> 0.00 mm
- net /mux_2: track 47.2 -> 0.00 mm
- net +3V3: track 50.9 -> 3.93 mm
- net /mux_1: track 45.8 -> 0.00 mm
- net /mux_3: track 40.3 -> 0.00 mm
- net /ESP32/EN: track 38.0 -> 0.00 mm
- net Net-(J26-Pin_1): track 25.5 -> 0.00 mm
- net /pwd_D0: track 0.00 -> 23.4 mm
- net /pwd_4: track 0.00 -> 23.2 mm
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- removed copper zone on B.Cu, net /led_cluster/led_cur_lim/DOWN_OUT
- removed copper zone on F.Cu, net /led_cluster/led_cur_lim/DOWN_OUT
- removed copper zone on B.Cu, net /led_cluster/led_cur_lim/UP_OUT
- removed copper zone on F.Cu, net /led_cluster/led_cur_lim/UP_OUT
- removed copper zone on B.Cu, net /led_cluster/led_cur_lim1/DOWN_OUT
- removed copper zone on F.Cu, net /led_cluster/led_cur_lim1/DOWN_OUT
- removed copper zone on B.Cu, net /led_cluster/led_cur_lim1/UP_OUT
- removed copper zone on F.Cu, net /led_cluster/led_cur_lim1/UP_OUT
- removed copper zone on B.Cu, net /led_cluster/led_cur_lim2/DOWN_OUT
- removed copper zone on F.Cu, net /led_cluster/led_cur_lim2/DOWN_OUT
- removed copper zone on B.Cu, net /led_cluster/led_cur_lim2/UP_OUT
- removed copper zone on F.Cu, net /led_cluster/led_cur_lim2/UP_OUT
- removed copper zone on B.Cu, net /led_cluster/led_cur_lim3/DOWN_OUT
- removed copper zone on F.Cu, net /led_cluster/led_cur_lim3/DOWN_OUT
- removed copper zone on B.Cu, net /led_cluster/led_cur_lim3/UP_OUT
- removed copper zone on F.Cu, net /led_cluster/led_cur_lim3/UP_OUT
- removed copper zone on B.Cu, net /led_cluster/led_cur_lim4/DOWN_OUT
- removed copper zone on F.Cu, net /led_cluster/led_cur_lim4/DOWN_OUT
- removed copper zone on B.Cu, net /led_cluster/led_cur_lim4/UP_OUT
- removed copper zone on F.Cu, net /led_cluster/led_cur_lim4/UP_OUT
- removed copper zone on B.Cu, net /led_cluster1/led_cur_lim/DOWN_OUT
- removed copper zone on F.Cu, net /led_cluster1/led_cur_lim/DOWN_OUT
- removed copper zone on B.Cu, net /led_cluster1/led_cur_lim/UP_OUT
- removed copper zone on F.Cu, net /led_cluster1/led_cur_lim/UP_OUT
- removed copper zone on B.Cu, net /led_cluster1/led_cur_lim1/DOWN_OUT
- removed copper zone on F.Cu, net /led_cluster1/led_cur_lim1/DOWN_OUT
- removed copper zone on B.Cu, net /led_cluster1/led_cur_lim1/UP_OUT
- removed copper zone on F.Cu, net /led_cluster1/led_cur_lim1/UP_OUT
- removed copper zone on B.Cu, net /led_cluster1/led_cur_lim2/DOWN_OUT
- removed copper zone on F.Cu, net /led_cluster1/led_cur_lim2/DOWN_OUT
- removed copper zone on B.Cu, net /led_cluster1/led_cur_lim2/UP_OUT
- removed copper zone on F.Cu, net /led_cluster1/led_cur_lim2/UP_OUT
- removed copper zone on B.Cu, net /led_cluster1/led_cur_lim3/DOWN_OUT
- removed copper zone on F.Cu, net /led_cluster1/led_cur_lim3/DOWN_OUT
- removed copper zone on B.Cu, net /led_cluster1/led_cur_lim3/UP_OUT
- removed copper zone on F.Cu, net /led_cluster1/led_cur_lim3/UP_OUT
- removed copper zone on B.Cu, net /led_cluster1/led_cur_lim4/DOWN_OUT
- removed copper zone on F.Cu, net /led_cluster1/led_cur_lim4/DOWN_OUT
- removed copper zone on B.Cu, net /led_cluster1/led_cur_lim4/UP_OUT
- removed copper zone on F.Cu, net /led_cluster1/led_cur_lim4/UP_OUT
- removed copper zone on B.Cu, net /led_cur_lim7/DOWN_OUT
- removed copper zone on F.Cu, net /led_cur_lim7/DOWN_OUT
- removed copper zone on B.Cu, net /led_cur_lim7/UP_OUT
- removed copper zone on F.Cu, net /led_cur_lim7/UP_OUT
- removed copper zone on B.Cu, net /led_cur_lim8/DOWN_OUT
- removed copper zone on F.Cu, net /led_cur_lim8/DOWN_OUT
- removed copper zone on B.Cu, net /led_cur_lim8/UP_OUT
- removed copper zone on F.Cu, net /led_cur_lim8/UP_OUT
- removed copper zone on B.Cu, net /out_B0
- removed copper zone on F.Cu, net /out_B0
- removed copper zone on B.Cu, net /out_B1
- removed copper zone on F.Cu, net /out_B1
- removed copper zone on F.Cu, net 230VAC
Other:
- board outline removed
